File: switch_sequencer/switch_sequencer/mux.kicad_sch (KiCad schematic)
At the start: 9 parts, among them J11 3.5mm_Mono_Switched_sm, U1 TMUX4051PWR, U13 TL072

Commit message: sequential switch wip more more
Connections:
- net GNDA is gone; now on net GND: J11.2 (SHEILD), J11.3 (SW), U13.5 (+)
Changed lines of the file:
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@@
 	(paper "A4")
-	(junction
-		(at 199.39 33.02)
-		(diameter 0)
-		(color 0 0 0 0)
-	)
 	(junction
 		(at 274.32 59.69)
@@
 	(junction
 		(at 243.84 41.91)
+		(diameter 0)
+		(color 0 0 0 0)
+	)
+	(junction
+		(at 199.39 33.02)
 		(diameter 0)
 		(color 0 0 0 0)
@@
 				(path "/1090b42d-0526-4901-ae26-1a4493d10820/4c22d006-f8e0-4fe5-9164-b59b12367ed8"
 					(reference "R44")
+					(unit 1)
+				)
+			)
+		)
+	)
+	(symbol
+		(lib_id "4ms_Power-symbol:GND")
+		(at 199.39 33.02 0)
+		(unit 1)
+		(exclude_from_sim no)
+		(in_bom yes)
+		(on_board yes)
+		(dnp no)
+		(property "Reference" "#PWR051"
+			(at 199.39 39.37 0)
+			(effects
+				(font
+					(size 1.27 1.27)
+				)
+				(hide yes)
+			)
+		)
+		(property "Value" "GND"
+			(at 199.39 36.83 0)
+			(effects
+				(font
+					(size 1.27 1.27)
+				)
+			)
+		)
+		(property "Footprint" ""
+			(at 199.39 33.02 0)
+			(effects
+				(font
+					(size 1.27 1.27)
+				)
+				(hide yes)
+			)
+		)
+		(property "Datasheet" ""
+			(at 199.39 33.02 0)
+			(effects
+				(font
+					(size 1.27 1.27)
+				)
+				(hide yes)
+			)
+		)
+		(property "Description" ""
+			(at 199.39 33.02 0)
+			(effects
+				(font
+					(size 1.27 1.27)
+				)
+				(hide yes)
+			)
+		)
+		(pin "1"
+		)
+		(instances
+			(project "switch_sequencer"
+				(path "/1090b42d-0526-4901-ae26-1a4493d10820/4c22d006-f8e0-4fe5-9164-b59b12367ed8"
+					(reference "#PWR051")
 					(unit 1)
 				)
@@
 	)
 	(symbol
-		(lib_id "4ms_Power-symbol:GNDA")
-		(at 254 44.45 180)
-		(unit 1)
-		(exclude_from_sim no)
-		(in_bom yes)
-		(on_board yes)
-		(dnp no)
-		(fields_autoplaced yes)
-		(property "Reference" "#PWR087"
-			(at 254 38.1 0)
-			(effects
-				(font
-					(size 1.27 1.27)
-				)
-				(hide yes)
-			)
-		)
-		(property "Value" "GNDA"
-			(at 254 39.37 0)
-			(effects
-				(font
-					(size 1.27 1.27)
-				)
-			)
-		)
-		(property "Footprint" ""
-			(at 254 44.45 0)
-			(effects
-				(font
-					(size 1.27 1.27)
-				)
-				(hide yes)
-			)
-		)
-		(property "Datasheet" ""
-			(at 254 44.45 0)
-			(effects
-				(font
-					(size 1.27 1.27)
-				)
-				(hide yes)
-			)
-		)
-		(property "Description" "(analog) ground power-flag symbol"
-			(at 254 44.45 0)
-			(effects
-				(font
-					(size 1.27 1.27)
-				)
-				(hide yes)
-			)
-		)
-		(pin "1"
-		)
-		(instances
-			(project "switch_sequencer"
-				(path "/1090b42d-0526-4901-ae26-1a4493d10820/4c22d006-f8e0-4fe5-9164-b59b12367ed8"
-					(reference "#PWR087")
-					(unit 1)
-				)
-			)
-		)
-	)
-	(symbol
-		(lib_id "4ms_Power-symbol:GNDA")
-		(at 199.39 33.02 0)
-		(unit 1)
-		(exclude_from_sim no)
-		(in_bom yes)
-		(on_board yes)
-		(dnp no)
-		(fields_autoplaced yes)
-		(property "Reference" "#PWR084"
-			(at 199.39 39.37 0)
-			(effects
-				(font
-					(size 1.27 1.27)
-				)
-				(hide yes)
-			)
-		)
-		(property "Value" "GNDA"
-			(at 199.39 38.1 0)
-			(effects
-				(font
-					(size 1.27 1.27)
-				)
-			)
-		)
-		(property "Footprint" ""
-			(at 199.39 33.02 0)
-			(effects
-				(font
-					(size 1.27 1.27)
-				)
-				(hide yes)
-			)
-		)
-		(property "Datasheet" ""
-			(at 199.39 33.02 0)
-			(effects
-				(font
-					(size 1.27 1.27)
-				)
-				(hide yes)
-			)
-		)
-		(property "Description" "(analog) ground power-flag symbol"
-			(at 199.39 33.02 0)
-			(effects
-				(font
-					(size 1.27 1.27)
-				)
-				(hide yes)
-			)
-		)
-		(pin "1"
-		)
-		(instances
-			(project "switch_sequencer"
-				(path "/1090b42d-0526-4901-ae26-1a4493d10820/4c22d006-f8e0-4fe5-9164-b59b12367ed8"
-					(reference "#PWR084")
-					(unit 1)
-				)
-			)
-		)
-	)
-	(symbol
 		(lib_id "TMUX4051:TMUX4051PWR")
 		(at 46.99 29.21 0)
@@
 					(unit 1)
 				)
+			)
+		)
+	)
+	(symbol
+		(lib_id "4ms_Power-symbol:GND")
+		(at 254 44.45 180)
+		(unit 1)
+		(exclude_from_sim no)
+		(in_bom yes)
+		(on_board yes)
+		(dnp no)
+		(property "Reference" "#PWR084"
+			(at 254 38.1 0)
+			(effects
+				(font
+					(size 1.27 1.27)
+				)
+				(hide yes)
+			)
+		)
+		(property "Value" "GND"
+			(at 254 40.64 0)
+			(effects
+				(font
+					(size 1.27 1.27)
+				)
+			)
+		)
+		(property "Footprint" ""
+			(at 254 44.45 0)
+			(effects
+				(font
+					(size 1.27 1.27)
+				)
+				(hide yes)
+			)
+		)
+		(property "Datasheet" ""
+			(at 254 44.45 0)
+			(effects
+				(font
+					(size 1.27 1.27)
+				)
+				(hide yes)
+			)
+		)
+		(property "Description" ""
+			(at 254 44.45 0)
+			(effects
+				(font
+					(size 1.27 1.27)
+				)
+				(hide yes)
+			)
+		)
+		(pin "1"
+		)
+		(instances
+			(project "switch_sequencer"
+				(path "/1090b42d-0526-4901-ae26-1a4493d10820/4c22d006-f8e0-4fe5-9164-b59b12367ed8"
+					(reference "#PWR084")
+					(unit 1)
+				)

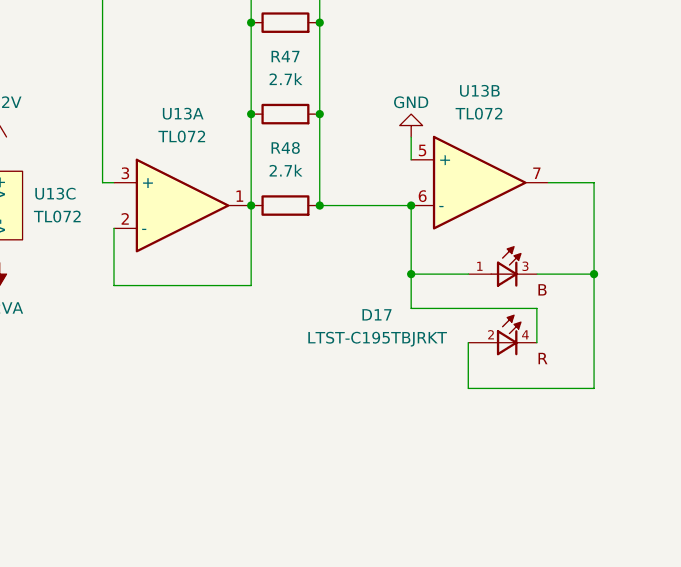
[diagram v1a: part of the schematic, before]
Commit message: sequential switch finished
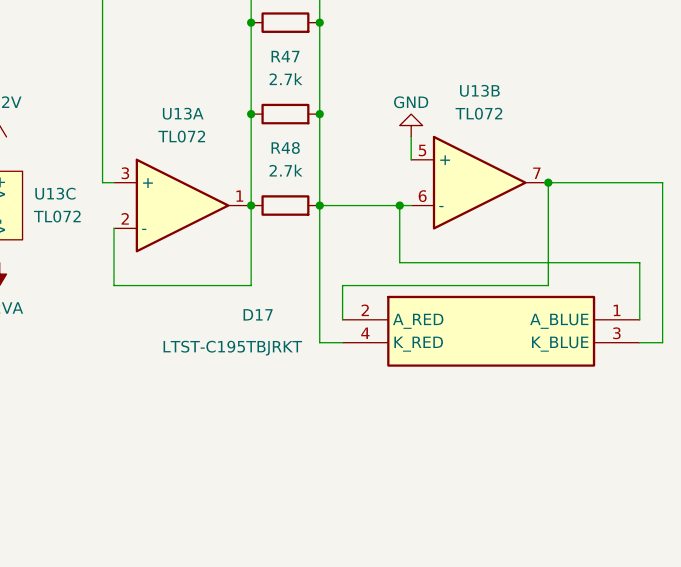
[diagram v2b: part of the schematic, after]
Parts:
- D17: footprint LTST-C195TBJRKT:LED_LTST-C195TBJRKT -> SamacSys_Parts:LTSTC195TBJRKT; symbol LTST-C195TBJRKT:LTST-C195TBJRKT -> SamacSys_Parts:LTST-C195TBJRKT; Height (none) -> 0.65; Manufacturer_Name (none) -> Lite-On; Manufacturer_Part_Number (none) -> LTST-C195TBJRKT; Mouser Part Number (none) -> 859-LTST-C195TBJRKT; Mouser Price/Stock (none) -> https://www.mouser.co.uk/ProductDetail/Lite-On/LTST-C195TBJ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
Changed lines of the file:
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@@
 	(paper "A4")
 	(junction
-		(at 274.32 59.69)
-		(diameter 0)
-		(color 0 0 0 0)
-	)
-	(junction
-		(at 254 52.07)
+		(at 269.24 49.53)
 		(diameter 0)
 		(color 0 0 0 0)
@@
 	)
 	(junction
-		(at 254 59.69)
+		(at 236.22 52.07)
 		(diameter 0)
 		(color 0 0 0 0)
 	)
 	(junction
-		(at 236.22 52.07)
+		(at 252.73 52.07)
 		(diameter 0)
 		(color 0 0 0 0)
@@
 	(wire
 		(pts
+			(xy 269.24 60.96) (xy 269.24 49.53)
+		)
+		(stroke
+			(width 0)
+			(type default)
+		)
+	)
+	(wire
+		(pts
 			(xy 222.25 22.86) (xy 219.71 22.86)
 		)
@@
 	(wire
 		(pts
-			(xy 243.84 52.07) (xy 254 52.07)
-		)
-		(stroke
-			(width 0)
-			(type default)
-		)
-	)
-	(wire
-		(pts
 			(xy 220.98 60.96) (xy 236.22 60.96)
 		)
@@
 	(wire
 		(pts
+			(xy 246.38 60.96) (xy 269.24 60.96)
+		)
+		(stroke
+			(width 0)
+			(type default)
+		)
+	)
+	(wire
+		(pts
 			(xy 195.58 72.39) (xy 201.93 72.39)
 		)
@@
 	(wire
 		(pts
-			(xy 274.32 49.53) (xy 269.24 49.53)
+			(xy 279.4 67.31) (xy 281.94 67.31)
+		)
+		(stroke
+			(width 0)
+			(type default)
+		)
+	)
+	(wire
+		(pts
+			(xy 269.24 49.53) (xy 281.94 49.53)
 		)
 		(stroke
@@
 	(wire
 		(pts
+			(xy 246.38 67.31) (xy 243.84 67.31)
+		)
+		(stroke
+			(width 0)
+			(type default)
+		)
+	)
+	(wire
+		(pts
+			(xy 252.73 52.07) (xy 254 52.07)
+		)
+		(stroke
+			(width 0)
+			(type default)
+		)
+	)
+	(wire
+		(pts
+			(xy 243.84 52.07) (xy 252.73 52.07)
+		)
+		(stroke
+			(width 0)
+			(type default)
+		)
+	)
+	(wire
+		(pts
 			(xy 109.22 72.39) (xy 129.54 72.39)
 		)
@@
 	(wire
 		(pts
-			(xy 274.32 59.69) (xy 274.32 49.53)
-		)
-		(stroke
-			(width 0)
-			(type default)
-		)
-	)
-	(wire
-		(pts
-			(xy 254 59.69) (xy 254 63.5)
-		)
-		(stroke
-			(width 0)
-			(type default)
-		)
-	)
-	(wire
-		(pts
-			(xy 267.97 63.5) (xy 267.97 67.31)
-		)
-		(stroke
-			(width 0)
-			(type default)
-		)
-	)
-	(wire
-		(pts
-			(xy 274.32 59.69) (xy 267.97 59.69)
+			(xy 281.94 67.31) (xy 281.94 49.53)
+		)
+		(stroke
+			(width 0)
+			(type default)
+		)
+	)
+	(wire
+		(pts
+			(xy 246.38 64.77) (xy 246.38 60.96)
+		)
+		(stroke
+			(width 0)
+			(type default)
+		)
+	)
+	(wire
+		(pts
+			(xy 252.73 58.42) (xy 252.73 52.07)
+		)
+		(stroke
+			(width 0)
+			(type default)
+		)
+	)
+	(wire
+		(pts
+			(xy 243.84 67.31) (xy 243.84 52.07)
+		)
+		(stroke
+			(width 0)
+			(type default)
+		)
+	)
+	(wire
+		(pts
+			(xy 279.4 64.77) (xy 279.4 58.42)
 		)
 		(stroke
@@
 	(wire
 		(pts
-			(xy 260.35 67.31) (xy 260.35 72.39)
-		)
-		(stroke
-			(width 0)
-			(type default)
-		)
-	)
-	(wire
-		(pts
-			(xy 274.32 72.39) (xy 274.32 59.69)
+			(xy 279.4 58.42) (xy 252.73 58.42)
 		)
 		(stroke
@@
 	(wire
 		(pts
-			(xy 254 59.69) (xy 254 52.07)
-		)
-		(stroke
-			(width 0)
-			(type default)
-		)
-	)
-	(wire
-		(pts
 			(xy 236.22 41.91) (xy 236.22 52.07)
 		)
@@
 	(wire
 		(pts
-			(xy 260.35 59.69) (xy 254 59.69)
-		)
-		(stroke
-			(width 0)
-			(type default)
-		)
-	)
-	(wire
-		(pts
 			(xy 109.22 104.14) (xy 129.54 104.14)
 		)
@@
 	(wire
 		(pts
-			(xy 260.35 72.39) (xy 274.32 72.39)
-		)
-		(stroke
-			(width 0)
-			(type default)
-		)
-	)
-	(wire
-		(pts
 			(xy 205.74 33.02) (xy 199.39 33.02)
 		)
@@
 		(pts
 			(xy 219.71 22.86) (xy 217.17 22.86)
-		)
-		(stroke
-			(width 0)
-			(type default)
-		)
-	)
-	(wire
-		(pts
-			(xy 254 63.5) (xy 267.97 63.5)
 		)
 		(stroke
@@
 	)
 	(symbol
-		(lib_id "LTST-C195TBJRKT:LTST-C195TBJRKT")
-		(at 262.89 64.77 0)
+		(lib_id "SamacSys_Parts:LTST-C195TBJRKT")
+		(at 246.38 64.77 0)
 		(unit 1)
 		(exclude_from_sim no)
@@
 		(dnp no)
 		(property "Reference" "D17"
-			(at 250.19 64.262 0)
+			(at 236.982 64.262 0)
 			(effects
 				(font
@@
 		)
 		(property "Value" "LTST-C195TBJRKT"
-			(at 250.19 66.802 0)
-			(effects
-				(font
-					(size 1.27 1.27)
-				)
-			)
-		)
-		(property "Footprint" "LTST-C195TBJRKT:LED_LTST-C195TBJRKT"
-			(at 262.89 64.77 0)
+			(at 226.314 67.056 0)
+			(effects
+				(font
+					(size 1.27 1.27)
+				)
+				(justify left top)
+			)
+		)
+		(property "Footprint" "SamacSys_Parts:LTSTC195TBJRKT"
+			(at 275.59 159.69 0)
+			(effects
+				(font
+					(size 1.27 1.27)
+				)
+				(justify left top)
+				(hide yes)
+			)
+		)
+		(property "Datasheet" "https://optoelectronics.liteon.com/upload/download/DS22-2001-079/LTST-C195TBJRKT%20.pdf"
+			(at 275.59 259.69 0)
+			(effects
+				(font
+					(size 1.27 1.27)
+				)
+				(justify left top)
+				(hide yes)
+			)
+		)
+		(property "Description" "LED,SMD,0605,Bi-Colour,Blue/Red Lite-On LTST-C195TBJRKT Bi-colour Blue, Red LED, 470 / 631 nm, 4-Pin 1513 (0605), Rectangle Lens SMD Package"
+			(at 246.38 64.77 0)
+			(effects
+				(font
+					(size 1.27 1.27)
+				)
+				(hide yes)
+			)
+		)
+		(property "PARTREV" ""
+			(at 246.38 64.77 0)
 			(effects
 				(font
@@
 			)
 		)
-		(property "Datasheet" ""
-			(at 262.89 64.77 0)
-			(effects
-				(font
-					(size 1.27 1.27)
-				)
-				(hide yes)
-			)
-		)
-		(property "Description" ""
-			(at 262.89 64.77 0)
-			(effects
-				(font
-					(size 1.27 1.27)
-				)
-				(hide yes)
-			)
-		)
-		(property "PARTREV" ""
-			(at 262.89 64.77 0)
+		(property "MANUFACTURER" "Lite-On Inc."
+			(at 246.38 64.77 0)
 			(effects
 				(font
@@
 			)
 		)
-		(property "MANUFACTURER" "Lite-On Inc."
-			(at 262.89 64.77 0)
+		(property "STANDARD" "Manufacturer Recommendation"
+			(at 246.38 64.77 0)
 			(effects
 				(font
@@
 			)
 		)
-		(property "STANDARD" "Manufacturer Recommendation"
-			(at 262.89 64.77 0)
-			(effects
-				(font
-					(size 1.27 1.27)
-				)
-				(justify bottom)
-				(hide yes)
-			)
+		(property "Height" "0.65"
+			(at 275.59 459.69 0)
+			(effects
+				(font
+					(size 1.27 1.27)
+				)
+				(justify left top)
+				(hide yes)
+			)
+		)
+		(property "Mouser Part Number" "859-LTST-C195TBJRKT"
+			(at 275.59 559.69 0)
+			(effects
+				(font
+					(size 1.27 1.27)
+				)
+				(justify left top)
+				(hide yes)
+			)
+		)
+		(property "Mouser Price/Stock" "https://www.mouser.co.uk/ProductDetail/Lite-On/LTST-C195TBJRKT?qs=zkxzjn%2FNGl5uy8%252BmRt4Q0Q%3D%3D"
+			(at 275.59 659.69 0)
+			(effects
+				(font
+					(size 1.27 1.27)
+				)
+				(justify left top)
+				(hide yes)
+			)
+		)
+		(property "Manufacturer_Name" "Lite-On"
+			(at 275.59 759.69 0)
+			(effects
+				(font
+					(size 1.27 1.27)
+				)
+				(justify left top)
+				(hide yes)
+			)
+		)
+		(property "Manufacturer_Part_Number" "LTST-C195TBJRKT"
+			(at 275.59 859.69 0)
+			(effects
+				(font
+					(size 1.27 1.27)
+				)
+				(justify left top)
+				(hide yes)
+			)
